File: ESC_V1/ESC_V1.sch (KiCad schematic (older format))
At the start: 27 parts, among them J1 Conn_01x06_Female, J2 Conn_01x03_Female, J3 Conn_01x02_Female, Q1 NPN Transistor 40V, Q10 NPN Transistor 40V, Q11 P Channel 40V 30A, Q12 N Channel 40V 30A, Q2 NPN Transistor 40V, Q3 P Channel 40V 30A, Q4 N Channel 40V 30A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

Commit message: Board v2 with darlington array and higher current capacity
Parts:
- removed J2: Conn_01x03_Female, Connector_PinHeader_2.54mm:PinHeader_1x03_P2.54mm_Vertical, symbol Connector:Conn_01x03_Female
- removed J3: Conn_01x02_Female, Connector_PinHeader_2.54mm:PinHeader_1x02_P2.54mm_Vertical, symbol Connector:Conn_01x02_Female
- removed Q1, Q10, Q2, Q5, Q6, Q9: NPN Transistor 40V, Package_TO_SOT_SMD:SOT-23, symbol Device:Q_NPN_BEC
- removed R1, R2, R3, R4, R5, R6: 10k, Resistor_SMD:R_0603_1608Metric_Pad1.05x0.95mm_HandSolder, symbol Device:R_Small
- added J2, J3, J4: Conn_01x01_Female, TestPoint:TestPoint_Pad_3.0x3.0mm, symbol Connector:Conn_01x01_Female
- added J5, J6: Conn_01x01_Female, TestPoint:TestPoint_Pad_4.0x4.0mm, symbol Connector:Conn_01x01_Female
- added U1: ULN2803A, Package_SO:SOIC-18W_7.5x11.6mm_P1.27mm, symbol Transistor_Array:ULN2803A
- J1: value Conn_01x06_Female -> Conn_01x07_Female; footprint Connector_PinHeader_2.54mm:PinHeader_1x06_P2.54mm_Vertical -> Connector_PinSocket_2.54mm:PinSocket_1x07_P2.54mm_Vertical; symbol Connector:Conn_01x06_Female -> Connector:Conn_01x07_Female
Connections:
- net IN1 is gone; now on net GND: J1.1 (Pin_1)
- net GND: now also J6.1 (Pin_1), U1.9 (GND)
- net OUT1: now also Q3.1 (G), U1.18 (O1); no longer D1.2 (A), D2.1 (K), Q3.2 (D), Q4.3 (D)
- net OUT2: now also Q4.1 (G), U1.17 (O2); no longer D3.2 (A), D4.1 (K), Q7.2 (D), Q8.3 (D)
- net OUT3: now also Q7.1 (G), U1.16 (O3); no longer D5.2 (A), D6.1 (K), Q11.2 (D), Q12.3 (D)
- net VCC: now also J5.1 (Pin_1), U1.10 (COM)
- net OUT4: now reaches Q8.1 (G)
- net OUT4: now also U1.15 (O4)
- net OUT5: now reaches Q11.1 (G)
- net OUT5: now also U1.14 (O5)
- net OUT6: now reaches Q12.1 (G)
- net OUT6: now also U1.13 (O6)
- net IN2: no longer names the net of J1.2 (Pin_2)
- net IN2: now also U1.6 (I6)
- net IN3: no longer names the net of J1.3 (Pin_3)
- net IN3: now also U1.5 (I5)
- net IN4: no longer names the net of J1.4 (Pin_4)
- net IN4: now also U1.4 (I4)
- net IN5: no longer names the net of J1.5 (Pin_5)
- net IN5: now also U1.3 (I3)
- net IN6: no longer names the net of J1.6 (Pin_6)
- net IN6: now also U1.2 (I2)
- new net: J1.7 (Pin_7), U1.1 (I1)
- new net MOTOR1: D1.2 (A), D2.1 (K), J2.1 (Pin_1), Q3.2 (D), Q4.3 (D)
- new net MOTOR2: D3.2 (A), D4.1 (K), J3.1 (Pin_1), Q7.2 (D), Q8.3 (D)
- new net MOTOR3: D5.2 (A), D6.1 (K), J4.1 (Pin_1), Q11.2 (D), Q12.3 (D)
- no-connect marks 0 -> 4

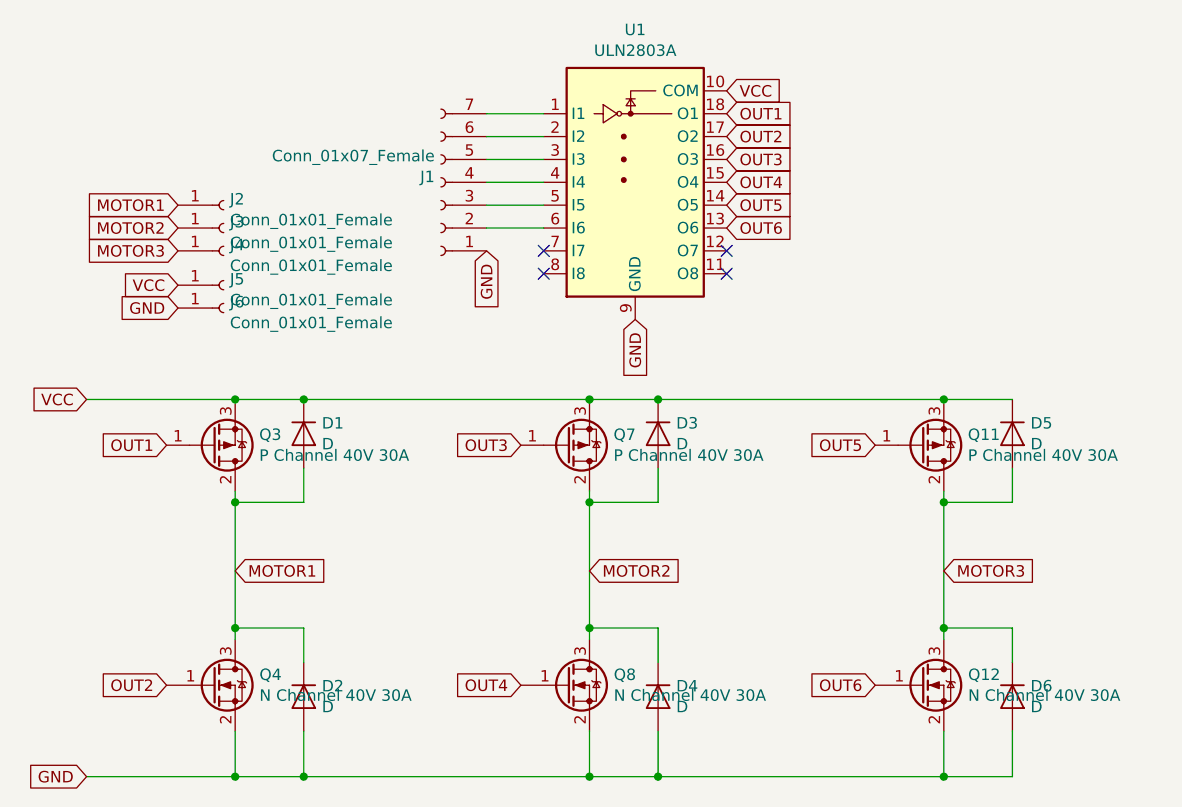
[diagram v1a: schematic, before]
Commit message: FETs moved but no bridge drivers yet
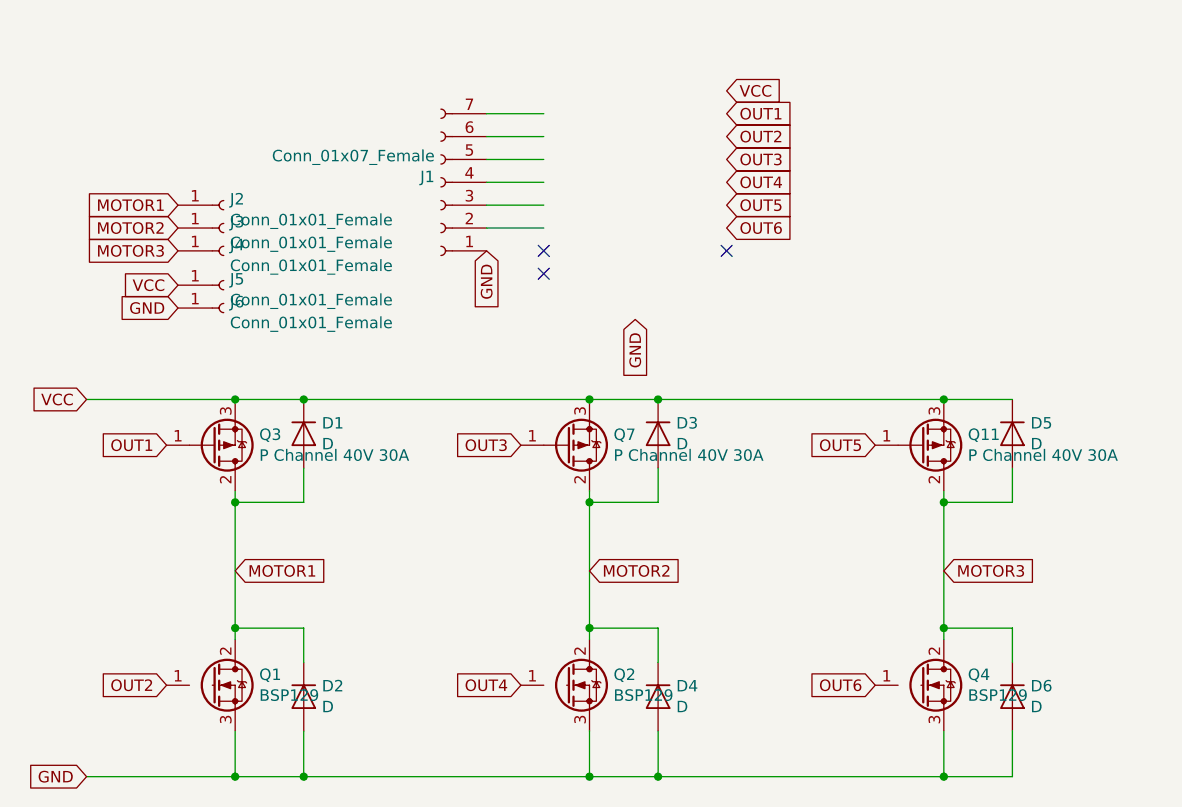
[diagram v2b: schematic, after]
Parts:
- removed Q12, Q4, Q8: N Channel 40V 30A, Package_TO_SOT_SMD:TO-252-2, symbol Transistor_FET:2N7002
- removed U1: ULN2803A, Package_SO:SOIC-18W_7.5x11.6mm_P1.27mm, symbol Transistor_Array:ULN2803A
- added Q1, Q2, Q4: BSP129, Package_TO_SOT_SMD:TO-252-2, symbol Transistor_FET:BSP129
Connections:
- no-connect marks 4 -> 3
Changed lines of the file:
@@
-$EndComp
-$Comp
-L Transistor_FET:2N7002 Q4
-U 1 1 5E436BE9
-P 3350 3500
-F 0 "Q4" H 3556 3546 50  0000 L CNN
-F 1 "N Channel 40V 30A" H 3556 3455 50  0000 L CNN
-F 2 "Package_TO_SOT_SMD:TO-252-2" H 3550 3425 50  0001 L CIN
-F 3 "https://www.fairchildsemi.com/datasheets/2N/2N7002.pdf" H 3350 3500 50  0001 L CNN
-	1    3350 3500
-	1    0    0    -1
 $EndComp
 $Comp
@@
 $EndComp
 $Comp
-L Transistor_FET:2N7002 Q8
-U 1 1 5E4385C6
-P 4900 3500
-F 0 "Q8" H 5106 3546 50  0000 L CNN
-F 1 "N Channel 40V 30A" H 5106 3455 50  0000 L CNN
-F 2 "Package_TO_SOT_SMD:TO-252-2" H 5100 3425 50  0001 L CIN
-F 3 "https://www.fairchildsemi.com/datasheets/2N/2N7002.pdf" H 4900 3500 50  0001 L CNN
-	1    4900 3500
-	1    0    0    -1
-$EndComp
-$Comp
 L Device:D D3
 U 1 1 5E4385CD
@@
 Connection ~ 3750 3900
 Connection ~ 3750 2250
-$Comp
-L Transistor_FET:2N7002 Q12
-U 1 1 5E4396D3
-P 6450 3500
-F 0 "Q12" H 6656 3546 50  0000 L CNN
-F 1 "N Channel 40V 30A" H 6656 3455 50  0000 L CNN
-F 2 "Package_TO_SOT_SMD:TO-252-2" H 6650 3425 50  0001 L CIN
-F 3 "https://www.fairchildsemi.com/datasheets/2N/2N7002.pdf" H 6450 3500 50  0001 L CNN
-	1    6450 3500
-	1    0    0    -1
-$EndComp
 $Comp
 L Device:D D5
@@
 Text GLabel 3200 1600 0    50   Input ~ 0
 MOTOR3
-$Comp
-L Transistor_Array:ULN2803A U1
-U 1 1 5E4446DB
-P 5200 1200
-F 0 "U1" H 5200 1767 50  0000 C CNN
-F 1 "ULN2803A" H 5200 1676 50  0000 C CNN
-F 2 "Package_SO:SOIC-18W_7.5x11.6mm_P1.27mm" H 5250 550 50  0001 L CNN
-F 3 "http://www.ti.com/lit/ds/symlink/uln2803a.pdf" H 5300 1000 50  0001 C CNN
-	1    5200 1200
-	1    0    0    -1
-$EndComp
 NoConn ~ 4800 1600
 NoConn ~ 4800 1700
 NoConn ~ 5600 1600
-NoConn ~ 5600 1700
 Text GLabel 5200 1900 3    50   Input ~ 0
 GND
@@
 Text GLabel 4550 1600 3    50   Input ~ 0
 GND
+$Comp
+L Transistor_FET:BSP129 Q1
+U 1 1 5E57629A
+P 3350 3500
+F 0 "Q1" H 3555 3546 50  0000 L CNN
+F 1 "BSP129" H 3555 3455 50  0000 L CNN
+F 2 "Package_TO_SOT_SMD:TO-252-2" H 3550 3425 50  0001 L CIN
+F 3 "https://www.infineon.com/dgdl/Infineon-BSP129-DS-v01_42-en.pdf?fileId=db3a30433c1a8752013c1fc296d2395f" H 3350 3500 50  0001 L CNN
+	1    3350 3500
+	1    0    0    -1
+$EndComp
+$Comp
+L Transistor_FET:BSP129 Q2
+U 1 1 5E576A18
+P 4900 3500
+F 0 "Q2" H 5105 3546 50  0000 L CNN
+F 1 "BSP129" H 5105 3455 50  0000 L CNN
+F 2 "Package_TO_SOT_SMD:TO-252-2" H 5100 3425 50  0001 L CIN
+F 3 "https://www.infineon.com/dgdl/Infineon-BSP129-DS-v01_42-en.pdf?fileId=db3a30433c1a8752013c1fc296d2395f" H 4900 3500 50  0001 L CNN
+	1    4900 3500
+	1    0    0    -1
+$EndComp
+$Comp
+L Transistor_FET:BSP129 Q4
+U 1 1 5E5771A5
+P 6450 3500
+F 0 "Q4" H 6655 3546 50  0000 L CNN
+F 1 "BSP129" H 6655 3455 50  0000 L CNN
+F 2 "Package_TO_SOT_SMD:TO-252-2" H 6650 3425 50  0001 L CIN
+F 3 "https://www.infineon.com/dgdl/Infineon-BSP129-DS-v01_42-en.pdf?fileId=db3a30433c1a8752013c1fc296d2395f" H 6450 3500 50  0001 L CNN
+	1    6450 3500
+	1    0    0    -1
+$EndComp
 $EndSCHEMATC
